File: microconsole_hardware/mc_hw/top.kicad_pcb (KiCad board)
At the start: 2 copper layers, 161 x 96 mm, 112 parts, among them J1 USB_C_Receptacle_USB2.0_16P, Q1 DMP2035U-7, Q2 DMP2035U-7, SW10 TL3301NF160QG, SW11 TL3301NF160QG, SW12 TL3301NF160QG, SW13 TL3301NF160QG, SW14 TL3301NF160QG, SW15 TL3301NF160QG, SW16 Joystick, SW17 Joystick, SW19 SPDT_Slide_PTH_11.6x4.0mm, SW2 TL3301NF160QG, SW3 TL3301NF160QG, SW4 TL3301NF160QG, SW5 TL3301NF160QG, SW6 TL3301NF160QG, SW7 TL3301NF160QG, SW8 TL3301NF160QG, SW9 TL3301NF160QG, U1 MCP73833-FCI/UN, U2 S2B-PH-K-S, U3 MCP23017-E/SO, U4 ADS7828E/2K5, U5 PCM5102APWR, U6 PAM8302AADCR, U7 PAM8406DR

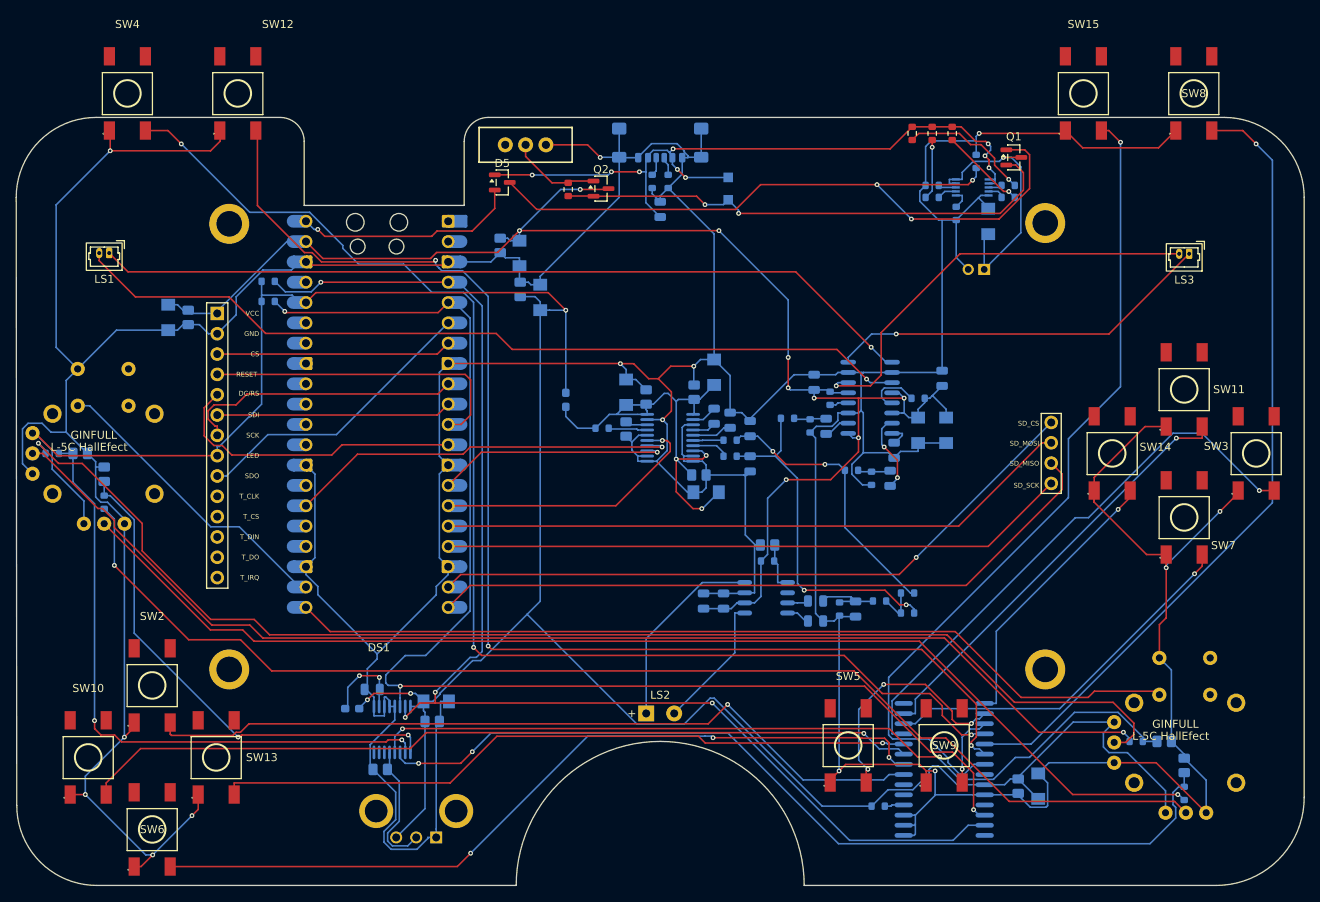
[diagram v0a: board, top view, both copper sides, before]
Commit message: add battery sense and thermistor
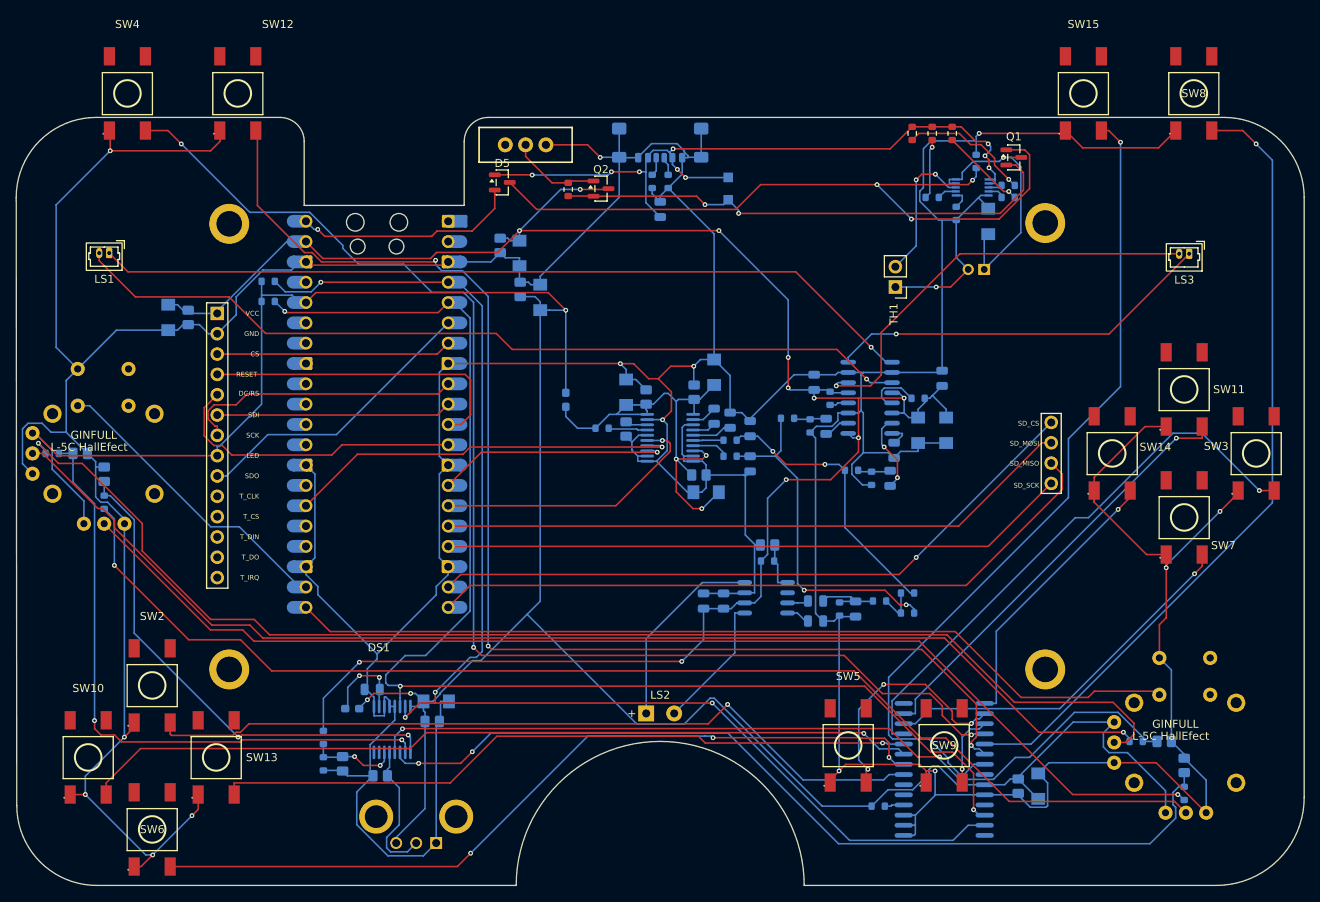
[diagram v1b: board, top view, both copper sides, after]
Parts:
- removed R10: 10k, PCM_SparkFun-Resistor:R_0603_1608Metric
- added C51: 100nF 50V X7R, project_parts:C_0805_2012Metric_KEMET_IPC-B, B.Cu at (109.8, 138.8)
- added R32: 68k 1%, PCM_SparkFun-Resistor:R_0603_1608Metric, B.Cu at (107.4, 135.5)
- added R33: 82k 1%, PCM_SparkFun-Resistor:R_0603_1608Metric, B.Cu at (107.4, 138.8)
- added TH1: Vishay NTCLE201E3103SBA, Connector_PinHeader_2.54mm:PinHeader_1x02_P2.54mm_Vertical, F.Cu at (178.9, 79.2)
- moved C44 0.80 mm to (114.5, 140.3)
- moved RV1 0.70 mm to (121.5, 148.7)
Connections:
- U4 pad 6: unconnected-(U4-CH5-Pad6) -> BAT_SENSE
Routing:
- net AMP_VDD: track 194.5 -> 253.0 mm, vias 9 -> 11
- net GND: track 906.0 -> 924.7 mm, vias 14 -> 15
- net Net-(U1-THERM): track 2.43 -> 17.9 mm, vias 0 -> 2
- net BAT_SENSE: track 0.00 -> 11.1 mm, vias 0 -> 2
- net VOL_ADC: track 16.7 -> 17.7 mm

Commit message: Fix usb
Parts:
- removed J1: USB_C_Receptacle_USB2.0_16P, Connector_USB:USB_C_Receptacle_GCT_USB4135-GF-A_6P_TopMnt_Horizontal
- added J2: USB_C_Receptacle, Connector_USB:USB_C_Receptacle_HCTL_HC-TYPE-C-16P-01A, B.Cu at (148.4, 60.7)
- C1: moved to F.Cu
- moved C1 9.36 mm to (148.4, 60.2)
- moved R3 1.75 mm to (147.2, 67.2)
- moved R4 1.18 mm to (150.4, 67.2)
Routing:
- net GND: track 924.7 -> 956.1 mm, vias 15 -> 14
- net USB-VBUS: track 89.5 -> 92.4 mm, vias 9 -> 7
- net IO1 / Left Stick Y: track 159.4 -> 157.0 mm
- net Net-(J2-CC2): track 2.54 -> 2.02 mm

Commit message: completely fix up board and schematic
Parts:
- D2, D3, D4: footprint PCM_SparkFun-Resistor:R_0603_1608Metric -> LED_SMD:LED_0603_1608Metric_Pad1.05x0.95mm_HandSolder
- moved C44 8.26 mm to (109.4, 146.8), turned to -90 degrees
- moved C51 3.96 mm to (113.7, 139.5), turned to 0 degrees
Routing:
- net GND: track 956.1 -> 942.9 mm, vias 14 -> 16
- net VOL_ADC: track 17.7 -> 23.9 mm
- net BAT_SENSE: track 11.1 -> 11.8 mm, vias 2 -> 0
- net 3v3: track 318.5 -> 319.2 mm

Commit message: drc
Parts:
- moved SW12 0.20 mm to (96.7, 55.2)
- moved SW15 0.10 mm to (202.4, 55.1)
- moved SW4 0.10 mm to (82.9, 55.1)
- moved SW8 0.10 mm to (216.2, 55.1)
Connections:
- A2 pad 39: AMP_VDD -> VSYS_BAT
- C29 pad 2: AMP_VDD -> VSYS_BAT
- C34 pad 2: AMP_VDD -> VSYS_BAT
- C35 pad 1: AMP_VDD -> VSYS_BAT
- C38 pad 1: AMP_VDD -> VSYS_BAT
- C39 pad 1: AMP_VDD -> VSYS_BAT
- C43 pad 2: AMP_VDD -> Net-(U7-PVDDR)
- C45 pad 2: AMP_VDD -> VSYS_BAT
- C46 pad 1: AMP_VDD -> VSYS_BAT
- C47 pad 2: AMP_VDD -> VSYS_BAT
- C48 pad 2: AMP_VDD -> VSYS_BAT
- DS1 pad 1: AMP_VDD -> VSYS_BAT
- Q2 pad 3: AMP_VDD -> VSYS_BAT
- R24 pad 1: AMP_VDD -> VSYS_BAT
- R25 pad 2: AMP_VDD -> VSYS_BAT
- R27 pad 1: AMP_VDD -> VSYS_BAT
- R32 pad 2: AMP_VDD -> VSYS_BAT
- U6 pad 6: AMP_VDD -> VSYS_BAT
- U7 pad 13: AMP_VDD -> Net-(U7-PVDDR)
- U7 pad 4: AMP_VDD -> VSYS_BAT
- U7 pad 6: AMP_VDD -> VSYS_BAT
- U7 pad 9: AMP_VDD -> VSYS_BAT
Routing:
- net AMP_VDD: track 253.0 -> 0.00 mm, vias 11 -> 0
- net (no net): track 0.00 -> 253.0 mm, vias 0 -> 11

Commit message: fixup things
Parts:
- C1: footprint PCM_SparkFun-Capacitor:C_0805_2012Metric -> project_parts:C_0805_2012Metric_KEMET_IPC-B
- C2: footprint project_parts:C1206 -> project_parts:C_0805_2012Metric_KEMET_IPC-B
- R18, R19: value 470 OHM -> 470
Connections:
- C43 pad 2: Net-(U7-PVDDR) -> VSYS_BAT
- U1 pad 1: USB-VBUS -> unconnected-(U1-VDD-Pad1)
- U1 pad 10: BAT+ -> unconnected-(U1-V_{BAT}-Pad10)
- U7 pad 13: Net-(U7-PVDDR) -> VSYS_BAT
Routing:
- net VSYS_BAT: track 0.00 -> 253.0 mm, vias 0 -> 11
- net (no net): track 253.0 -> 0.00 mm, vias 11 -> 0
- net Net-(U1-PROG): track 2.54 -> 1.45 mm
- net BAT+: track 33.6 -> 32.6 mm
- net USB-VBUS: track 92.4 -> 91.6 mm
- net GND: track 942.9 -> 943.6 mm
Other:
- board text added: "U1"

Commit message: fix2
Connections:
- U1 pad 1: unconnected-(U1-VDD-Pad1) -> USB-VBUS
- U1 pad 10: unconnected-(U1-V_{BAT}-Pad10) -> BAT+
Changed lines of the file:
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@@
 			)
 		)
-		(property ki_fp_filters "R_* RV_*")
+		(property ki_fp_filters "PinHeader_1x02_P2.54mm_*")
 		(sheetname "/Battery/")
 		(sheetfile "battery.kicad_sch")
@@
 		)
 		(embedded_fonts no)
-		(model "${KICAD8_3DMODEL_DIR}/Capacitor_SMD.3dshapes/C_0805_2012Metric.wrl"
+		(model "${KICAD10_3DMODEL_DIR}/Capacitor_SMD.3dshapes/C_0805_2012Metric.step"
 			(offset
 				(xyz 0 0 0)
@@
 		)
 		(embedded_fonts no)
-		(model "${KICAD8_3DMODEL_DIR}/Capacitor_SMD.3dshapes/C_0805_2012Metric.wrl"
+		(model "${KICAD10_3DMODEL_DIR}/Capacitor_SMD.3dshapes/C_0805_2012Metric.step"
 			(offset
 				(xyz 0 0 0)
@@
 			)
 		)
-		(property ki_fp_filters "SOT?23*")
+		(property ki_fp_filters "MSOP-10*")
 		(sheetname "/Battery/")
 		(sheetfile "battery.kicad_sch")
@@
 			(unit
 				(name "A")
-				(pins "9" "8" "6" "1" "5" "10" "2" "3" "4" "7")
+				(pins "9" "8" "6" "10" "5" "1" "2" "3" "4" "7")
 			)
 		)
@@
 			(size 0.3 1)
 			(layers "B.Cu")
-			(net "unconnected-(U1-VDD-Pad1)")
+			(net "USB-VBUS")
 			(pinfunction "VDD_1")
-			(pintype "power_in+no_connect")
+			(pintype "power_in")
 			(thermal_bridge_angle 0)
 		)
@@
 			(size 0.3 1)
 			(layers "B.Cu")
-			(net "unconnected-(U1-V_{BAT}-Pad10)")
+			(net "BAT+")
 			(pinfunction "V_{BAT}_10")
-			(pintype "power_out+no_connect")
+			(pintype "power_out")
 			(thermal_bridge_angle 0)
 		)
@@
 			)
 		)
-		(property "Datasheet" ""
+		(property "Datasheet" "https://assets.nexperia.com/documents/data-sheet/PMEG40T30ER.pdf"
 			(at 0 0 270)
 			(unlocked yes)
@@
 			)
 		)
-		(attr smd)
+		(attr smd dnp)
 		(duplicate_pad_numbers_are_jumpers no)
 		(fp_line

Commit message: fix up
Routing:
- net USB-VBUS: track 91.6 -> 92.1 mm
- net BAT+: track 32.6 -> 33.1 mm
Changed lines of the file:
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@@
 			(net "USB-VBUS")
 			(pinfunction "VDD_1")
-			(pintype "power_in")
+			(pintype "passive")
 			(thermal_bridge_angle 0)
 		)
@@
 			(net "BAT+")
 			(pinfunction "V_{BAT}_10")
-			(pintype "power_out")
+			(pintype "passive")
 			(thermal_bridge_angle 0)
 		)
@@
 			)
 		)
-		(property ki_fp_filters "TO-???* *_Diode_* *SingleDiode* D_*")
+		(property ki_fp_filters "TO-???* *_Diode_* *SingleDiode* D_* Diode_*")
 		(sheetname "/Battery/")
 		(sheetfile "battery.kicad_sch")
@@
 			)
 		)
-		(attr smd dnp)
+		(attr smd)
 		(duplicate_pad_numbers_are_jumpers no)
 		(fp_line
@@
 	)
 	(segment
+		(start 190.55 65.75)
+		(end 190.55 66.25)
+		(width 0.2)
+		(layer "B.Cu")
+		(net "USB-VBUS")
+	)
+	(segment
 		(start 191.3517 65.75)
 		(end 191.3517 65.0517)
@@
 		(width 0.2)
 		(layer "B.Cu")
+		(net "BAT+")
+	)
+	(segment
+		(start 186.45 65.75)
+		(end 186.45 66.25)
+		(width 0.2)
+		(layer "B.Cu")
